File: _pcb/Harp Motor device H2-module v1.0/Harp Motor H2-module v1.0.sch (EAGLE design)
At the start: 84 parts, among them IC1 FT232RL, IC10 OPA365, IC11 74LVC1G125DBV, IC12 74LVC1G125DBV, IC2 74LVC1G125DBV, IC3 LP5907MFX-3.3, IC7 USBLC6-2SC6, IC8 ATXMEGA32A4U, IC9 LP5907MFX-3.3, T1 DMG1012UW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

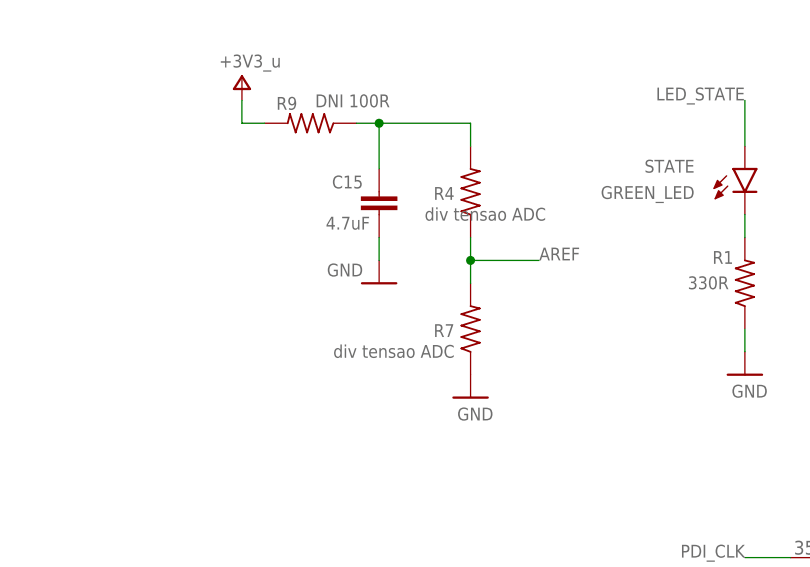
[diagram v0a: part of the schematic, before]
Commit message: Harp Motor device H2-module v1.0 - BOM updated
Harp Motor device H2-module v1.0 - BOM updated
- still missing component's codes
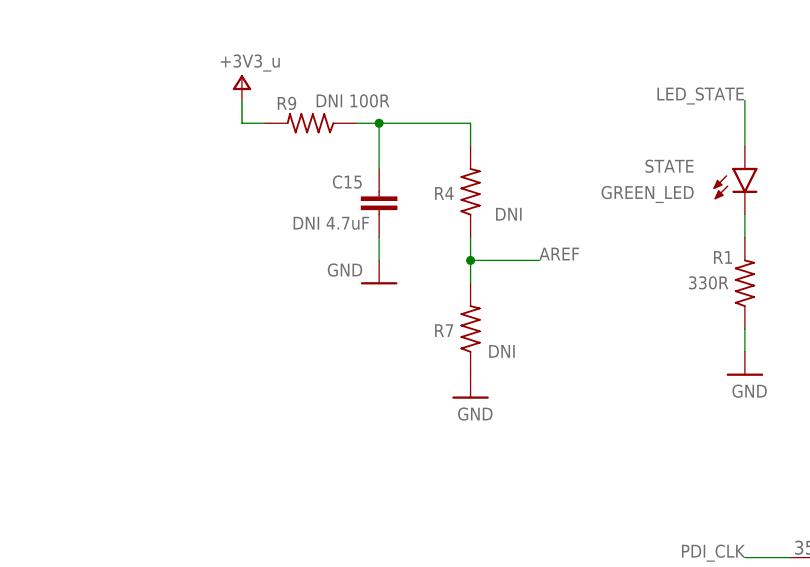
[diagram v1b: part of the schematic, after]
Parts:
- C15: value 4.7uF -> DNI 4.7uF
- R4: value div tensao ADC -> DNI; MPN n.a -> DNI; OEPS TBD -> DNI
- R7: value div tensao ADC -> DNI; MPN n.a. -> DNI; OEPS TBD -> DNI
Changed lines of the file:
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@@
 </part>
 <part name="R5" library="Harp Motor H2-module v1.0" deviceset="R-US_" device="R0402" value="10R">
-<attribute name="MPN" value="ERJ-PA2J100X
-"/>
-<attribute name="OEPS" value="OEPS020041
-"/>
+<attribute name="MPN" value="ERJ-PA2J100X "/>
+<attribute name="OEPS" value="OEPS020041 "/>
 </part>
 <part name="GND1" library="Harp Motor H2-module v1.0" deviceset="GND" device="">
@@
 <attribute name="OEPS" value="OEPS070026"/>
 </part>
-<part name="R4" library="Harp Motor H2-module v1.0" deviceset="R-US_" device="R0402" value="div tensao ADC">
-<attribute name="MPN" value="n.a"/>
-<attribute name="OEPS" value="TBD"/>
-</part>
-<part name="R7" library="Harp Motor H2-module v1.0" deviceset="R-US_" device="R0402" value="div tensao ADC">
-<attribute name="MPN" value="n.a."/>
-<attribute name="OEPS" value="TBD"/>
+<part name="R4" library="Harp Motor H2-module v1.0" deviceset="R-US_" device="R0402" value="DNI">
+<attribute name="MPN" value="DNI"/>
+<attribute name="OEPS" value="DNI"/>
+</part>
+<part name="R7" library="Harp Motor H2-module v1.0" deviceset="R-US_" device="R0402" value="DNI">
+<attribute name="MPN" value="DNI"/>
+<attribute name="OEPS" value="DNI"/>
 </part>
 <part name="GND13" library="Harp Motor H2-module v1.0" deviceset="GND" device=""/>
@@
 <attribute name="OEPS" value="OEPS010004"/>
 </part>
-<part name="C15" library="Harp Motor H2-module v1.0" deviceset="C-EU" device="C0603K" value="4.7uF">
+<part name="C15" library="Harp Motor H2-module v1.0" deviceset="C-EU" device="C0603K" value="DNI 4.7uF">
 <attribute name="MPN" value="C1608X6S1C475K080AC"/>
 <attribute name="OEPS" value="OEPS010018"/>
 </part>
 <part name="R9" library="Harp Motor H2-module v1.0" deviceset="R-US_" device="R0402" value="DNI 100R">
-<attribute name="MPN" value="ERJ-2RKF1000X
-"/>
+<attribute name="MPN" value="ERJ-2RKF1000X "/>
 <attribute name="OEPS" value="OEPS020004"/>
 </part>
@@
 <instance part="R4" gate="G$1" x="149.86" y="226.06" smashed="yes" rot="R90">
 <attribute name="NAME" x="148.082" y="226.5934" size="1.4224" layer="95" font="vector" ratio="12" rot="R180"/>
-<attribute name="VALUE" x="158.242" y="224.282" size="1.4224" layer="96" font="vector" ratio="12" rot="R180"/>
+<attribute name="VALUE" x="155.702" y="224.282" size="1.4224" layer="96" font="vector" ratio="12" rot="R180"/>
 <attribute name="MPN" x="149.86" y="226.06" size="1.778" layer="96" rot="R90" display="off"/>
 <attribute name="OEPS" x="149.86" y="226.06" size="1.778" layer="96" rot="R90" display="off"/>
@@
 <instance part="R7" gate="G$1" x="149.86" y="210.82" smashed="yes" rot="R90">
 <attribute name="NAME" x="148.082" y="211.3534" size="1.4224" layer="95" font="vector" ratio="12" rot="R180"/>
-<attribute name="VALUE" x="148.082" y="209.042" size="1.4224" layer="96" font="vector" ratio="12" rot="R180"/>
+<attribute name="VALUE" x="154.94" y="209.042" size="1.4224" layer="96" font="vector" ratio="12" rot="R180"/>
 <attribute name="MPN" x="149.86" y="210.82" size="1.778" layer="96" rot="R90" display="off"/>
 <attribute name="OEPS" x="149.86" y="210.82" size="1.778" layer="96" rot="R90" display="off"/>

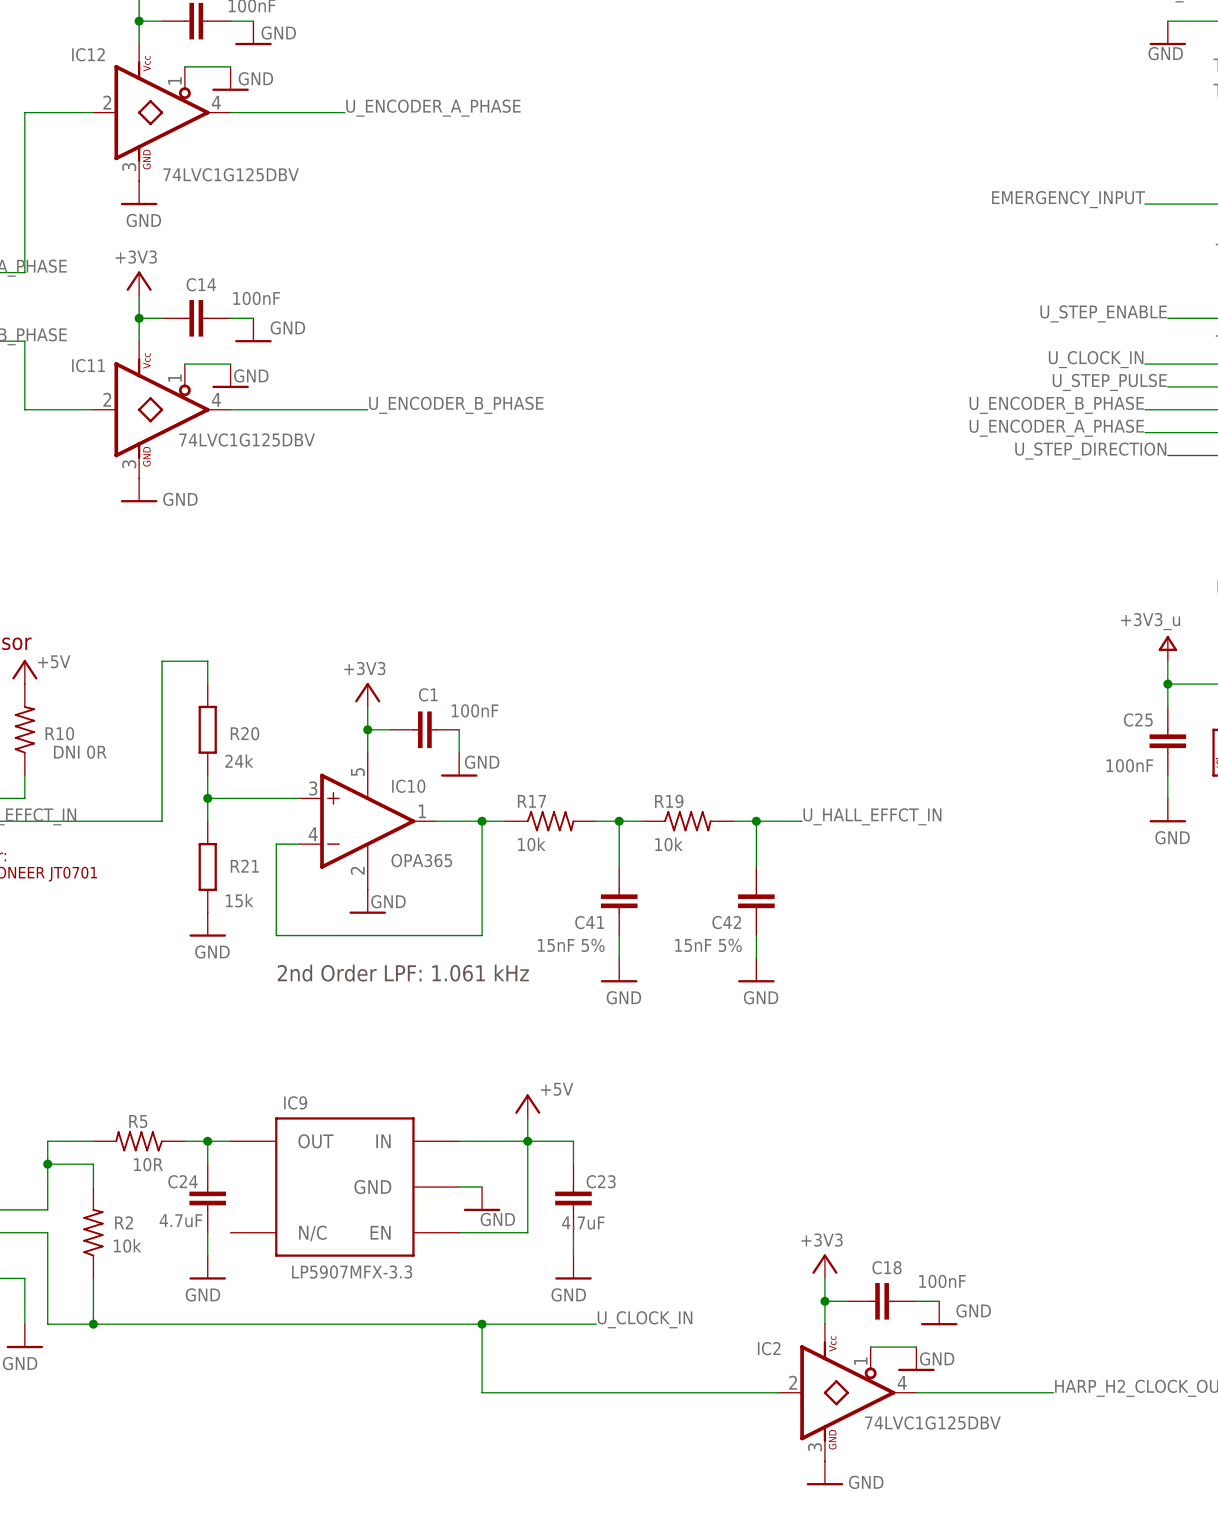
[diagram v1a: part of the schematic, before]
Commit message: Harp Motor device H2-module v1.0 BOM updated
Harp Motor device H2-module v1.0 BOM updated
- OEPS & MPN components code changed
- new BOM generated
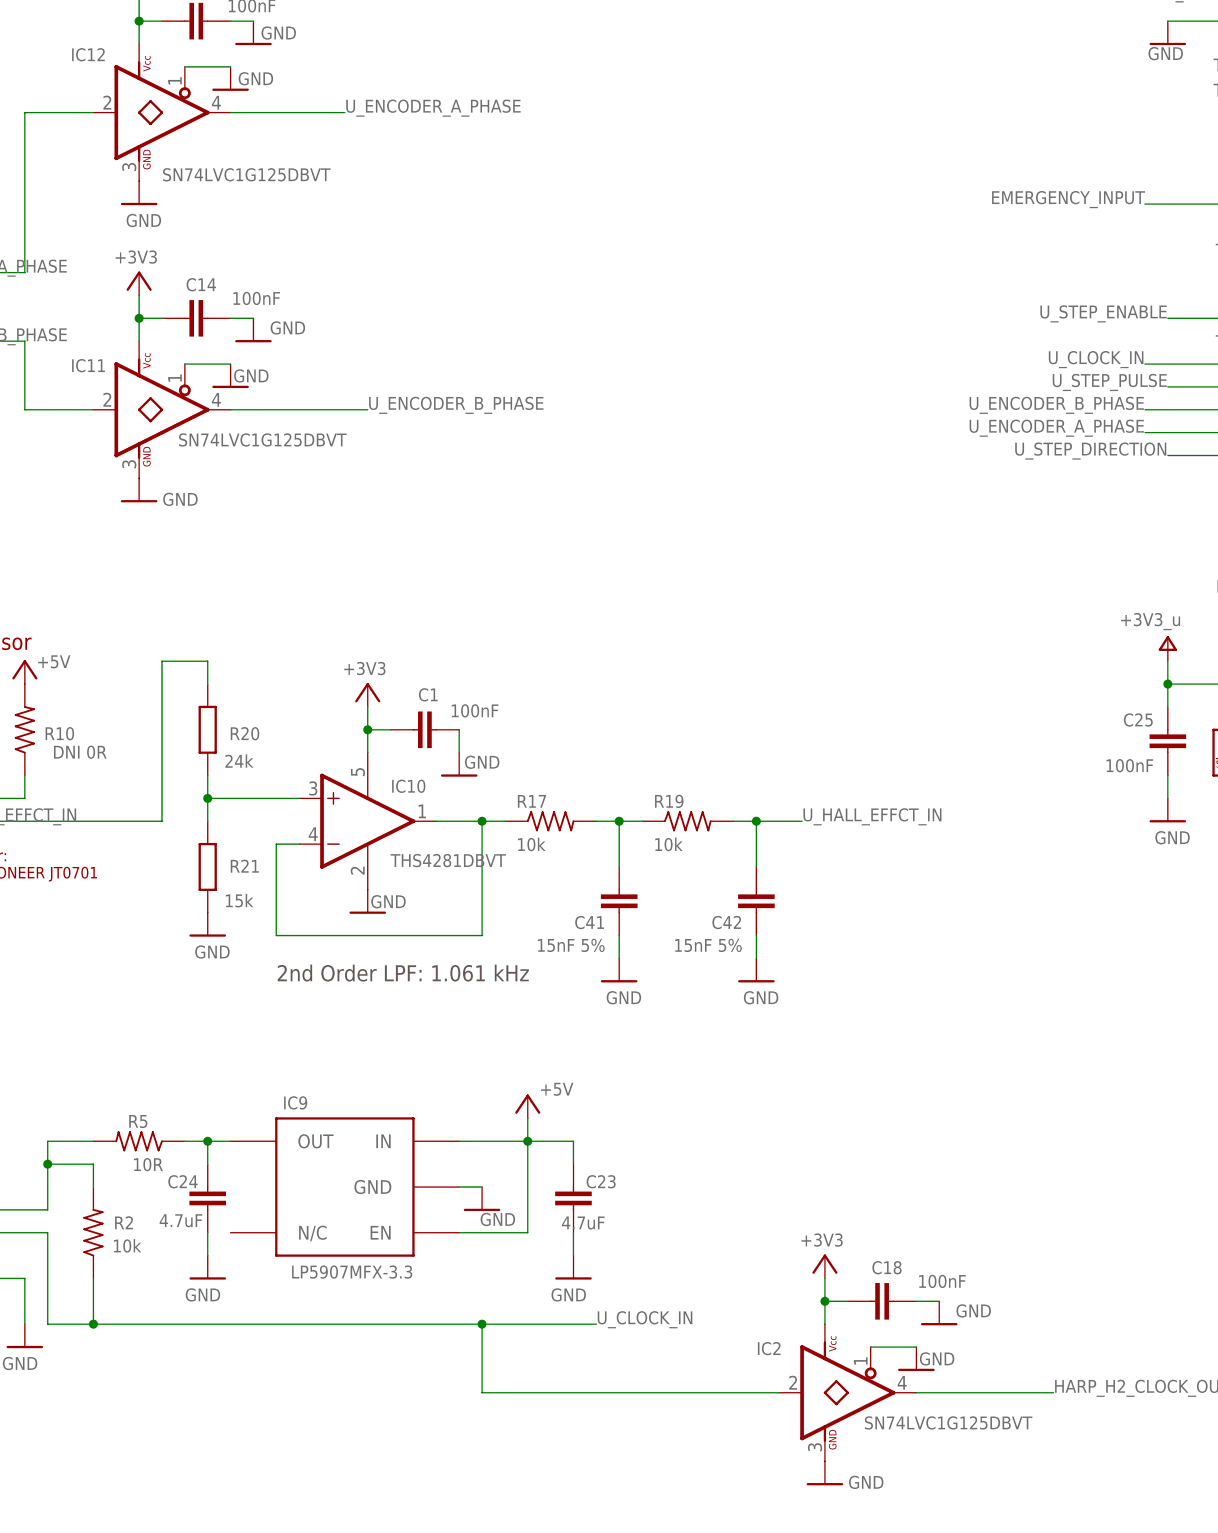
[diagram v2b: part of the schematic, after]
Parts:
- C13, C4, C6: OEPS OEPS080013 -> OEPS010011
- IC10: value OPA365 -> THS4281DBVT; MPN OEPS080019=TLV272CDGKR -> THS4281DBVT; OEPS TBD -> OEPS F01 068
- IC11, IC12, IC2: value 74LVC1G125DBV -> SN74LVC1G125DBVT
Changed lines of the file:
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@@
 <part name="C4" library="Harp Motor H2-module v1.0" deviceset="C-EU" device="C0402K" value="47pF">
 <attribute name="MPN" value="04025A470JAT2A"/>
-<attribute name="OEPS" value="OEPS080013"/>
+<attribute name="OEPS" value="OEPS010011"/>
 </part>
 <part name="C6" library="Harp Motor H2-module v1.0" deviceset="C-EU" device="C0402K" value="47pF">
 <attribute name="MPN" value="04025A470JAT2A"/>
-<attribute name="OEPS" value="OEPS080013"/>
+<attribute name="OEPS" value="OEPS010011"/>
 </part>
 <part name="L1" library="Harp Motor H2-module v1.0" deviceset="R-EU_" device="R0805" value="40R@100MHz">
@@
 <part name="C13" library="Harp Motor H2-module v1.0" deviceset="C-EU" device="C0402K" value="47pF">
 <attribute name="MPN" value="04025A470JAT2A"/>
-<attribute name="OEPS" value="OEPS080013"/>
+<attribute name="OEPS" value="OEPS010011"/>
 </part>
 <part name="TP4" library="Harp Motor H2-module v1.0" deviceset="TPSQ" device="TP11R" value="NO_COMPONENT"/>
@@
 <part name="GND13" library="Harp Motor H2-module v1.0" deviceset="GND" device=""/>
 <part name="VDD6" library="Harp Motor H2-module v1.0" deviceset="V+" device="" value="+3V3_u"/>
-<part name="IC11" library="Harp Motor H2-module v1.0" deviceset="74*1G125" device="DBV" technology="LVC">
+<part name="IC11" library="Harp Motor H2-module v1.0" deviceset="74*1G125" device="DBV" technology="LVC" value="SN74LVC1G125DBVT">
 <attribute name="MPN" value="SN74LVC1G125DBVT"/>
 <attribute name="OEPS" value="OEPS080029"/>
 </part>
-<part name="IC12" library="Harp Motor H2-module v1.0" deviceset="74*1G125" device="DBV" technology="LVC">
+<part name="IC12" library="Harp Motor H2-module v1.0" deviceset="74*1G125" device="DBV" technology="LVC" value="SN74LVC1G125DBVT">
 <attribute name="MPN" value="SN74LVC1G125DBVT"/>
 <attribute name="OEPS" value="OEPS080029"/>
@@
 </part>
 <part name="GND49" library="Harp Motor H2-module v1.0" deviceset="GND" device=""/>
-<part name="IC10" library="Harp Motor H2-module v1.0" deviceset="OPA365" device="">
-<attribute name="MPN" value="OEPS080019=TLV272CDGKR"/>
-<attribute name="OEPS" value="TBD"/>
+<part name="IC10" library="Harp Motor H2-module v1.0" deviceset="OPA365" device="" value="THS4281DBVT">
+<attribute name="MPN" value="THS4281DBVT"/>
+<attribute name="OEPS" value="OEPS F01 068"/>
 </part>
 <part name="+3V7" library="Harp Motor H2-module v1.0" deviceset="+3V3" device=""/>
@@
 </part>
 <part name="GND12" library="Harp Motor H2-module v1.0" deviceset="GND" device=""/>
-<part name="IC2" library="Harp Motor H2-module v1.0" deviceset="74*1G125" device="DBV" technology="LVC">
+<part name="IC2" library="Harp Motor H2-module v1.0" deviceset="74*1G125" device="DBV" technology="LVC" value="SN74LVC1G125DBVT">
 <attribute name="MPN" value="SN74LVC1G125DBVT"/>
 <attribute name="OEPS" value="OEPS080029"/>

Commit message: Harp Motor device H2-module v1.0 - BOM updated
Harp Motor device H2-module v1.0 - BOM updated
- new component codes on schematic
- new BOM generated
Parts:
- C41, C42: MPN TBD -> CGA2B3X7R1V153K050BB; OEPS TBD -> OEPS010023
- R20: MPN TBD -> ERJ-2RKF2402X; OEPS TBD -> OEPS020048
- X2, X5: OEPS TBD -> OEPS070041
- X3: OEPS TBD -> OEPS070020
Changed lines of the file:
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@@
 <part name="X3" library="Harp Motor H2-module v1.0" deviceset="22-23-2021" device="" value="1x2 case">
 <attribute name="MPN" value="282834-2"/>
-<attribute name="OEPS" value="TBD"/>
+<attribute name="OEPS" value="OEPS070020"/>
 </part>
 <part name="GND11" library="Harp Motor H2-module v1.0" deviceset="GND" device=""/>
@@
 <part name="X2" library="Harp Motor H2-module v1.0" deviceset="22-23-2051" device="" value="1x5 case">
 <attribute name="MPN" value="282834-5"/>
-<attribute name="OEPS" value="TBD"/>
+<attribute name="OEPS" value="OEPS070041"/>
 </part>
 <part name="GND16" library="Harp Motor H2-module v1.0" deviceset="GND" device=""/>
@@
 <part name="X5" library="Harp Motor H2-module v1.0" deviceset="22-23-2051" device="" value="1x5 case">
 <attribute name="MPN" value="282834-5"/>
-<attribute name="OEPS" value="TBD"/>
+<attribute name="OEPS" value="OEPS070041"/>
 </part>
 <part name="VDD5" library="Harp Motor H2-module v1.0" deviceset="V+" device="" value="+3V3_u"/>
@@
 </part>
 <part name="C41" library="Harp Motor H2-module v1.0" deviceset="C-EU" device="C0402K" value="15nF 5%">
-<attribute name="MPN" value="TBD"/>
-<attribute name="OEPS" value="TBD"/>
+<attribute name="MPN" value="CGA2B3X7R1V153K050BB"/>
+<attribute name="OEPS" value="OEPS010023"/>
 </part>
 <part name="GND45" library="Harp Motor H2-module v1.0" deviceset="GND" device=""/>
@@
 </part>
 <part name="C42" library="Harp Motor H2-module v1.0" deviceset="C-EU" device="C0402K" value="15nF 5%">
-<attribute name="MPN" value="TBD"/>
-<attribute name="OEPS" value="TBD"/>
+<attribute name="MPN" value="CGA2B3X7R1V153K050BB"/>
+<attribute name="OEPS" value="OEPS010023"/>
 </part>
 <part name="GND46" library="Harp Motor H2-module v1.0" deviceset="GND" device=""/>
@@
 <part name="GND48" library="Harp Motor H2-module v1.0" deviceset="GND" device=""/>
 <part name="R20" library="Harp Motor H2-module v1.0" deviceset="R-EU_" device="R0402" value="24k">
-<attribute name="MPN" value="TBD"/>
-<attribute name="OEPS" value="TBD"/>
+<attribute name="MPN" value="ERJ-2RKF2402X"/>
+<attribute name="OEPS" value="OEPS020048"/>
 </part>
 <part name="R21" library="Harp Motor H2-module v1.0" deviceset="R-EU_" device="R0402" value="15k">

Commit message: Harp Motor device H2-module v1.0 - BOM updated
Harp Motor device H2-module v1.0 - BOM updated
- THS4281DBVT OPES code updated: OEPS080038
- schematic updated
- BOM updated
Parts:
- IC10: OEPS OEPS F01 068 -> OEPS080038
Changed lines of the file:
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@@
 <part name="IC10" library="Harp Motor H2-module v1.0" deviceset="OPA365" device="" value="THS4281DBVT">
 <attribute name="MPN" value="THS4281DBVT"/>
-<attribute name="OEPS" value="OEPS F01 068"/>
+<attribute name="OEPS" value="OEPS080038"/>
 </part>
 <part name="+3V7" library="Harp Motor H2-module v1.0" deviceset="+3V3" device=""/>
